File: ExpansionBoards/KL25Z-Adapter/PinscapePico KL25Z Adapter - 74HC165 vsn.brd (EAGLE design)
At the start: 82.6 x 53.1 mm, 26 parts, among them IC1 SN74HC165DR, IC2 SN74HC165DR, IC3 SN74HC165DR, IC4 LIS3DHTR, IC5 ADS1115IDGSR, IC6 PCA9555APW,118, SW1 TS-1187A-B-A-B

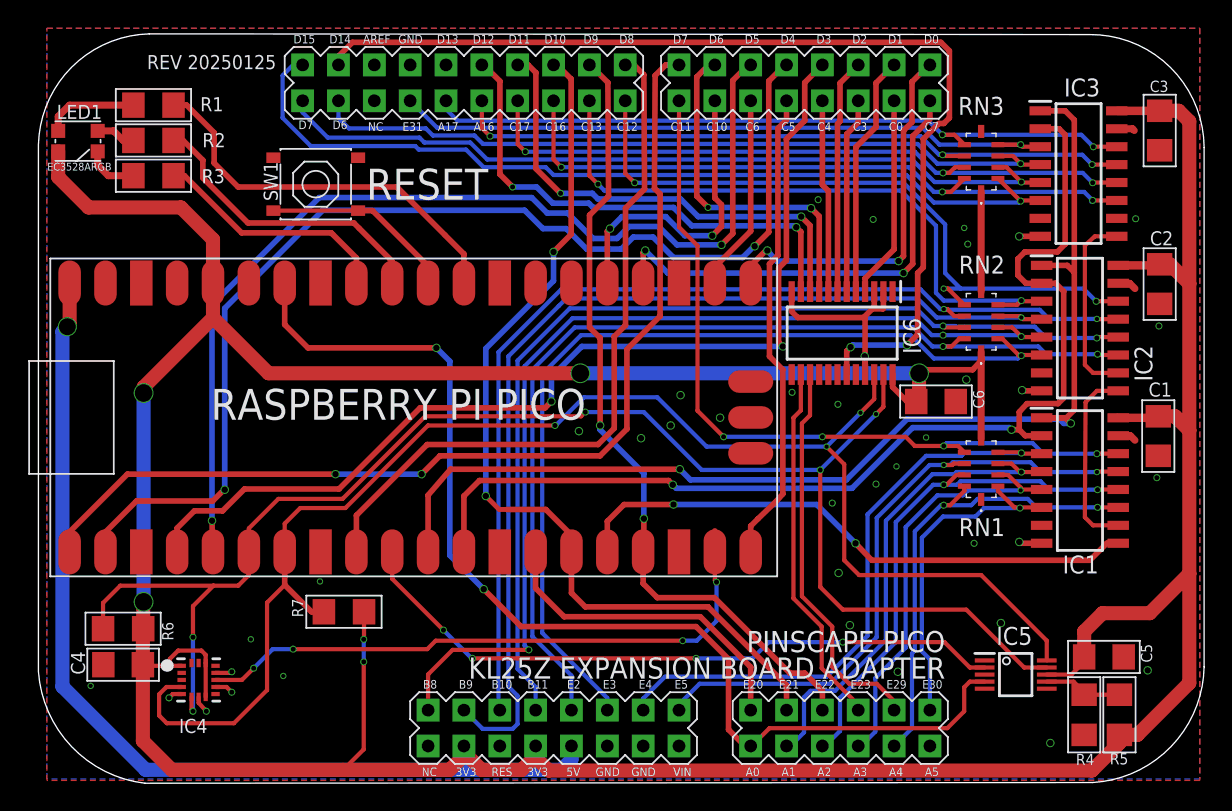
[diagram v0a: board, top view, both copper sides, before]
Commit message: Finish JSON configuration for 74HC165, tweaks to 74HC165 layout
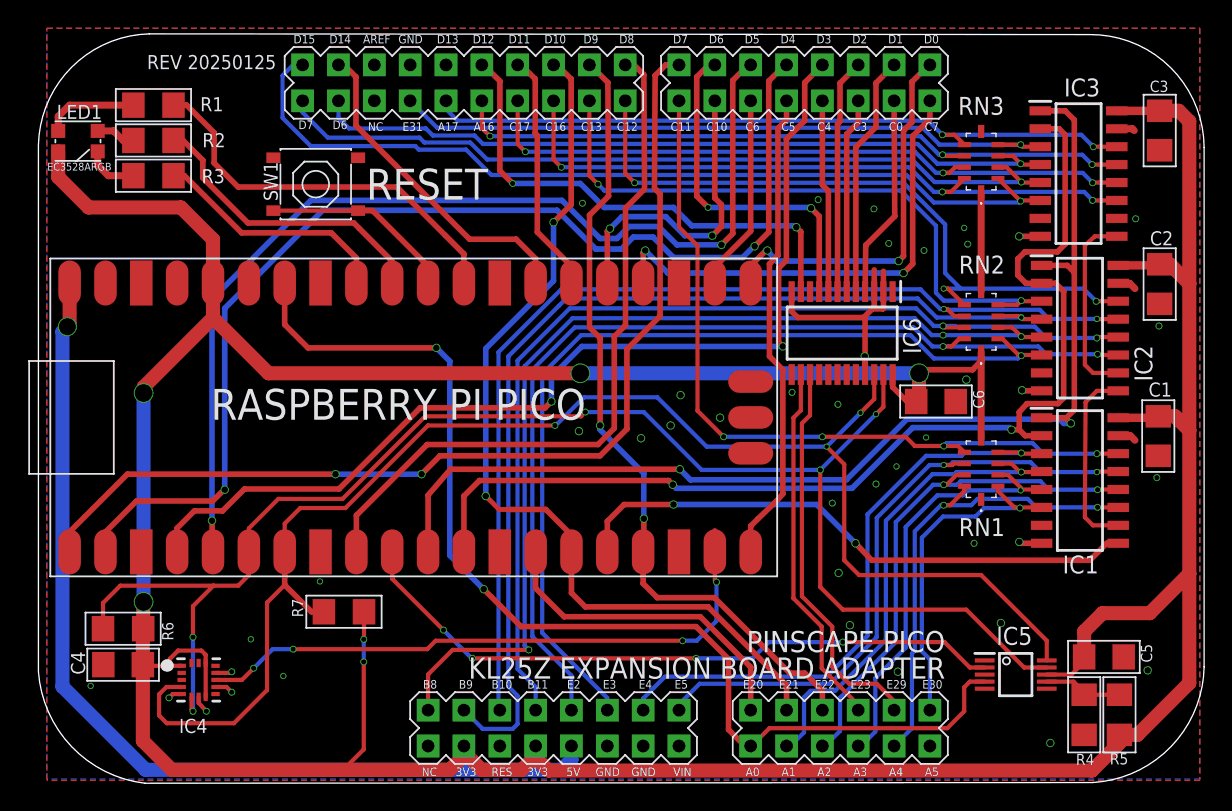
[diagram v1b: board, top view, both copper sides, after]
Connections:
- net PSU2_STATUS_SENSE: now also RASPBERRY_PI_PICO.GP20; no longer IC6.10
- net PSU2_STATUS_SET: now also RASPBERRY_PI_PICO.GP21; no longer IC6.19
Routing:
- net PSU2_STATUS_SET: track 73.0 -> 23.4 mm, vias 2 -> 0
- net PSU2_STATUS_SENSE: track 34.1 -> 17.2 mm, vias 2 -> 0
- net GND: track 29.0 -> 32.0 mm, vias 38 -> 41

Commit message: minor board updates
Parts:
- moved C5 2.81 mm to (75.7, 11.9)
- moved IC5 2.81 mm to (69.5, 10.7)
- moved R4 2.81 mm to (74.3, 7.80)
- moved R5 2.81 mm to (76.8, 7.80)
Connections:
- net BUTTON12: now also IC2.4, RN2.4; no longer IC2.13, RN2.8
- net BUTTON13: now also IC2.13, RN2.8; no longer IC2.4, RN2.4
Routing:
- net BUTTON12: track 73.7 -> 67.2 mm, vias 2 -> 1
- net PLUNGER_ADC: track 78.8 -> 81.8 mm
- net BUTTON13: track 72.6 -> 74.7 mm, vias 1 -> 2
- net 3V3_PICO: track 294.3 -> 296.3 mm, vias 6 -> 4
- net LED_B: track 28.3 -> 26.7 mm
- net PWM_GSCLK: track 27.4 -> 25.9 mm
- net SCL: track 104.8 -> 103.8 mm
- net CHIME_SCLK: track 80.7 -> 79.7 mm
- net PWM_XLAT: track 22.1 -> 22.7 mm
- net SDA: track 107.8 -> 107.2 mm
- net GND: vias 41 -> 45
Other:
- board text added: "REV 20250129"
- board text removed: "REV 20250125"

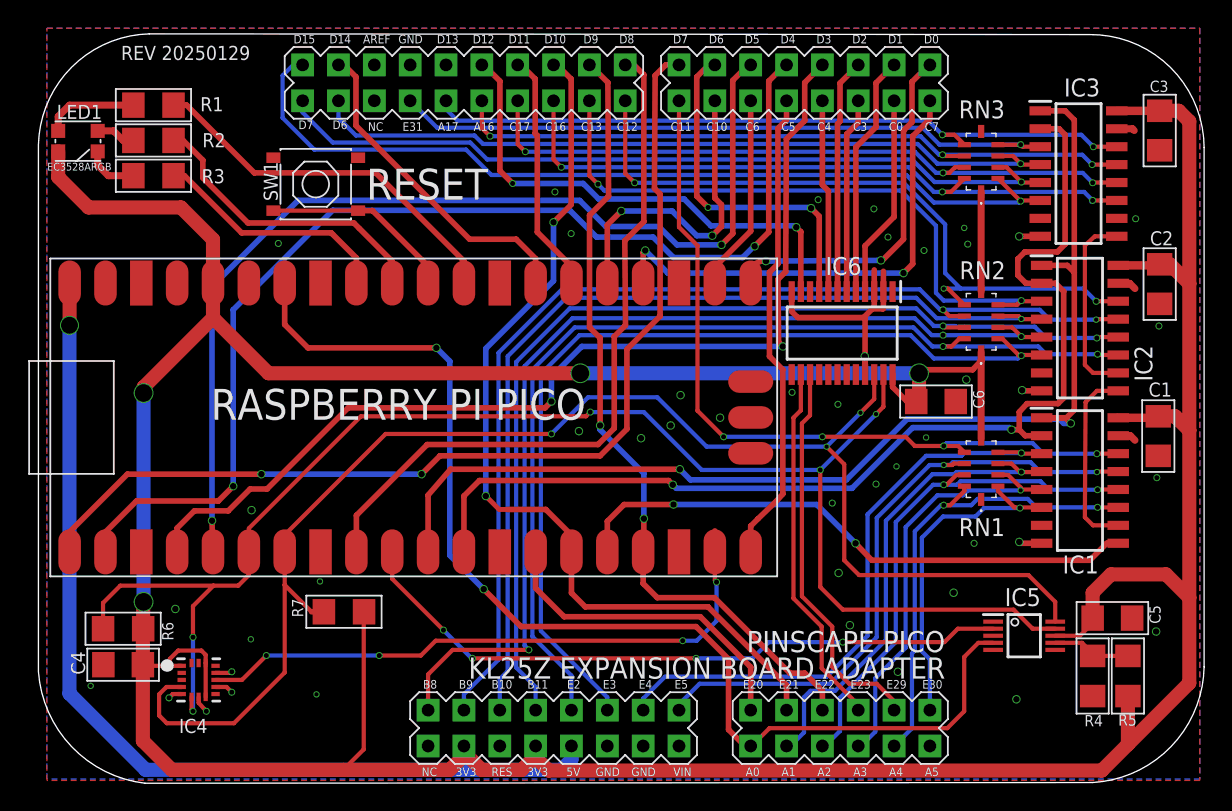
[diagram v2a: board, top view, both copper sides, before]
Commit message: THT version of the board design
- Changed Pico footprint to THT
- Relocated components
- Relayouted traces.
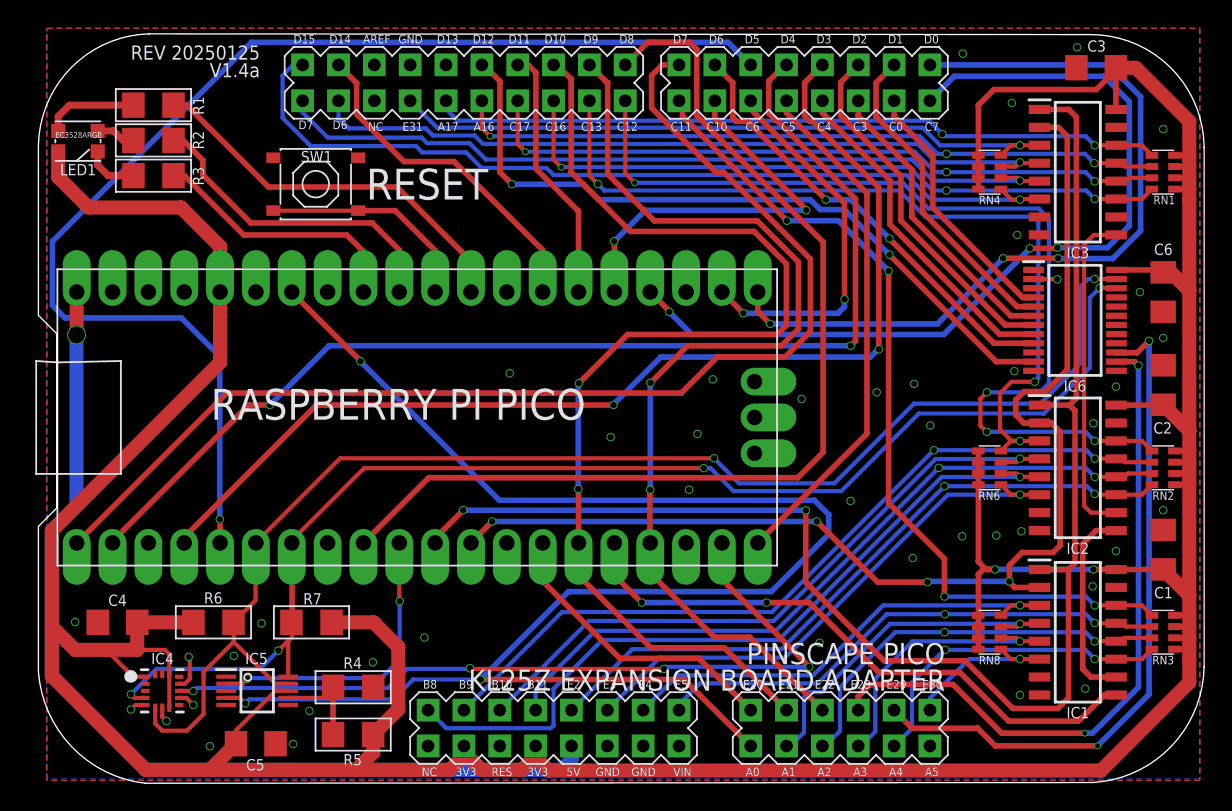
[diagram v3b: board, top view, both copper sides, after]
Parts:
- added RN4, RN6, RN8: CTS742C083, resistor-net:CTS742C083
- RASPBERRY_PI_PICO: device RaspberryPi_Pico:RPI_PICO -> RaspberryPi_Pico:RPI_PICO_TH
- RN1, RN2, RN3: value EXB-E10C103J -> CTS742C083; device SamacSys_Parts:EXBE10C103J -> resistor-net:CTS742C083
- moved C5 61.3 mm to (15.0, 3.00)
- moved R5 55.1 mm to (21.9, 3.65), turned to 180 degrees
- moved IC5 54.5 mm to (15.1, 6.75)
- moved R4 52.4 mm to (21.9, 7.00), turned to 180 degrees
- moved RN3 35.8 mm to (79.3, 10.9), turned to 270 degrees
- moved RN1 24.7 mm to (79.3, 43.5), turned to 270 degrees
- moved C6 17.9 mm to (79.3, 35.0), turned to 270 degrees
- moved RN2 16.5 mm to (79.3, 22.6), turned to 270 degrees
- moved IC6 16.5 mm to (73.0, 33.0), turned to 0 degrees
- moved IC1 10.8 mm to (73.2, 10.9)
- moved IC2 9.90 mm to (73.2, 22.6)
- moved C1 8.06 mm to (79.3, 16.8), turned to 90 degrees
- moved C2 7.15 mm to (79.3, 28.4), turned to 90 degrees
- moved R6 6.42 mm to (12.0, 11.6), turned to 0 degrees
- moved C3 6.33 mm to (74.5, 50.9), turned to 180 degrees
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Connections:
- removed net N$2: RN2.6, RN3.1
- net 3V3_PICO: now also RN1.5, RN1.7, RN1.8, RN2.5, RN2.6, RN2.7, RN2.8, RN3.5, RN3.6, RN3.7, RN3.8, RN4.1, RN4.2, RN4.3, RN4.4, RN6.1, RN6.2, RN6.3, RN6.4, RN8.1, RN8.2, RN8.3, RN8.4; no longer RN2.1
- net BUTTON1: now also RN3.4; no longer RN1.10
- net BUTTON10: now also RN2.4; no longer RN2.10
- net BUTTON11: now also RN2.3; no longer RN2.9
- net BUTTON12: now also RN6.7; no longer RN2.4
- net BUTTON13: now also RN2.2; no longer RN2.8
- net BUTTON14: now also RN6.6; no longer RN2.3
- net BUTTON15: now also RN2.1; no longer RN2.7
- net BUTTON16: now also RN6.8; no longer RN2.5
- net BUTTON17: now also RN1.4; no longer RN3.10
- net BUTTON18: now also RN1.3; no longer RN3.9
- net BUTTON19: now also RN1.2; no longer RN3.8
- net BUTTON2: now also RN8.6; no longer RN1.3
- net BUTTON20: now also RN1.1; no longer RN3.7
- net BUTTON21: now also RN4.8; no longer RN3.5
- net BUTTON22: now also RN4.7; no longer RN3.4
- net BUTTON23: now also RN4.6; no longer RN3.3
- net BUTTON24: now also RN4.5; no longer RN3.2
- net BUTTON3: now also RN3.3; no longer RN1.9
- net BUTTON4: now also RN8.7; no longer RN1.4
- net BUTTON5: now also RN8.5; no longer RN1.2
- net BUTTON6: now also RN3.1; no longer RN1.7
- net BUTTON7: now also RN3.2; no longer RN1.8
- net BUTTON8: now also RN8.8; no longer RN1.5
- net BUTTON9: now also RN6.5; no longer RN2.2
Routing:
- net PLUNGER_ADC: track 81.8 -> 114.9 mm, vias 2 -> 3
- net PWM_GSCLK: track 25.9 -> 57.0 mm, vias 2 -> 3
- net PWM_BLANK: track 34.3 -> 62.8 mm, vias 2 -> 3
- net BUTTON9: track 65.4 -> 38.6 mm
- net ADC_INTR: track 47.7 -> 21.3 mm, vias 4 -> 2
- net GND: track 32.0 -> 7.61 mm, vias 45 -> 43
- net PLUNGER_CAL_LED: track 25.9 -> 48.4 mm, vias 0 -> 2
- net IR_IN: track 51.0 -> 73.4 mm
- net BUTTON10: track 70.7 -> 48.9 mm
- net BUTTON_SHLD: track 83.1 -> 103.9 mm
- net PLUNGER_CAL_BTN: track 27.9 -> 48.4 mm, vias 0 -> 2
- net BUTTON12: track 67.2 -> 47.1 mm
- net BUTTON11: track 72.0 -> 52.0 mm
- net BUTTON15: track 49.6 -> 68.9 mm, vias 3 -> 4
- net BUTTON13: track 74.7 -> 56.7 mm
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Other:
- outline, holes or cut-outs redrawn
- board text added: "REV 20250125 V1.4a"
- board text removed: "REV 20250129"

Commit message: KL25Z adapter layout tweaks
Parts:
- RASPBERRY_PI_PICO: device RaspberryPi_Pico:RPI_PICO_TH -> RaspberryPi_Pico:RPI_PICO_TH_NO_DEBUG
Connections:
- net GND: no longer RASPBERRY_PI_PICO.GND@5
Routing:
- net PWM_GSCLK: track 57.0 -> 33.7 mm, vias 3 -> 1
- net PWM_BLANK: track 62.8 -> 44.1 mm, vias 3 -> 1
- net ACCEL_INTR: track 56.8 -> 44.8 mm, vias 4 -> 1
- net BUTTON15: track 68.9 -> 61.6 mm, vias 4 -> 2
- net GND: track 7.61 -> 10.8 mm, vias 43 -> 64
- net PWM_SIN: track 26.9 -> 24.2 mm, vias 2 -> 1
- net PLUNGER_SDA: track 21.2 -> 23.2 mm
- net PLUNGER_IRQ1_SCL: track 79.3 -> 80.7 mm
- net PLUNGER_ADC: track 114.9 -> 114.2 mm, vias 3 -> 6
- net PLUNGER_CAL_LED: track 48.4 -> 49.1 mm
- net BUTTON_DATA: track 42.9 -> 43.6 mm
- net BUTTON_SHLD: track 103.9 -> 103.3 mm, vias 2 -> 1
- net PLUNGER_IRQ2: track 70.9 -> 71.5 mm
- net BUTTON_CLK: track 84.3 -> 84.1 mm, vias 4 -> 3
- net PWM_XLAT: track 28.5 -> 28.7 mm, vias 2 -> 1
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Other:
- board text added: "REV 20250201"
- board text removed: "REV 20250125 V1.4a"

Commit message: KL25Z adapters - connect AGND to GND
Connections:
- net GND: now also RASPBERRY_PI_PICO.AGND
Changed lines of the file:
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@@
 <via x="64.35" y="5.1" extent="1-16" drill="0.35"/>
 <via x="33.75" y="8.075" extent="1-16" drill="0.45"/>
+<contactref element="RASPBERRY_PI_PICO" pad="AGND"/>
 </signal>
 <signal name="SDA">

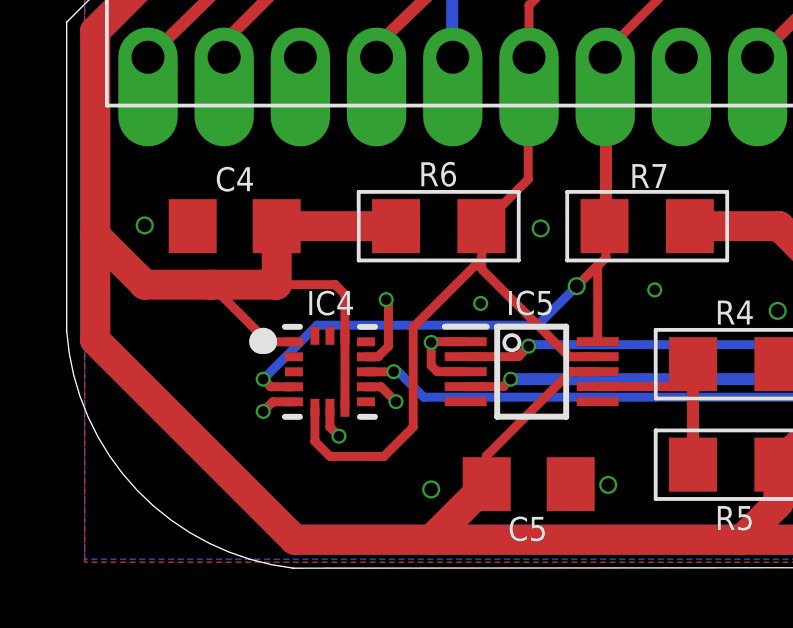
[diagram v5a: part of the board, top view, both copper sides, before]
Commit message: Update Pro and KL25Z adapter boards to make LIS3DH footprint compatible with LIS3DSH
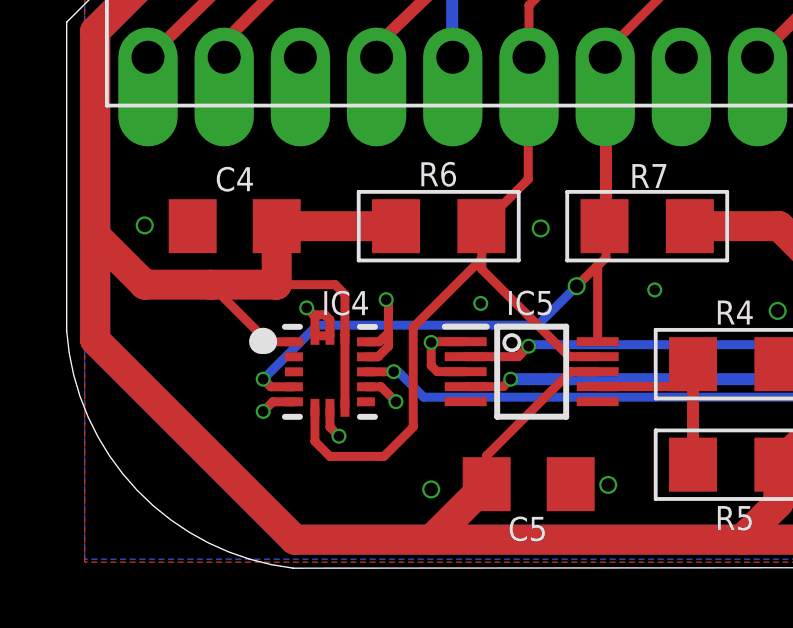
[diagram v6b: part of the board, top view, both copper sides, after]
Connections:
- net GND: now also IC4.13, IC4.15, IC4.16
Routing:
- net GND: track 10.8 -> 14.3 mm, vias 64 -> 65
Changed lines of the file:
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@@
 <attribute name="MOUSER_PART_NUMBER" value="511-LIS3DHTR" x="7.105" y="6.745" size="1.778" layer="27" display="off"/>
 <attribute name="MOUSER_PRICE-STOCK" value="https://www.mouser.co.uk/ProductDetail/STMicroelectronics/LIS3DHTR?qs=6la6oa3D8xzhXYax3cEo4w%3D%3D" x="7.105" y="6.745" size="1.778" layer="27" display="off"/>
-<attribute name="NAME" x="8.394" y="9.035" size="0.8" layer="25" align="center"/>
+<attribute name="NAME" x="8.894" y="9.035" size="0.8" layer="25" align="center"/>
 <attribute name="VALUE" x="8.394" y="4.405" size="0.7" layer="27" align="center"/>
 </element>
@@
 <wire x1="9.575" y1="7.245" x2="9.975" y2="7.245" width="0.3" layer="1"/>
 <wire x1="10.25" y1="9.15" x2="10.325" y2="9.075" width="0.3" layer="1"/>
-<wire x1="10.325" y1="9.075" x2="10.325" y2="7.595" width="0.3" layer="1"/>
+<wire x1="10.325" y1="9.075" x2="10.325" y2="8.05" width="0.3" layer="1"/>
 <via x="8.675" y="4.6" extent="1-16" drill="0.35"/>
 <via x="10.25" y="9.15" extent="1-16" drill="0.35"/>
 <via x="10.575" y="5.75" extent="1-16" drill="0.35"/>
 <contactref element="IC4" pad="7"/>
+<wire x1="10.325" y1="8.05" x2="10.325" y2="7.595" width="0.3" layer="1"/>
 <wire x1="8.375" y1="5.545" x2="8.375" y2="4.9" width="0.3" layer="1"/>
 <wire x1="8.675" y1="4.6" x2="8.375" y2="4.9" width="0.3" layer="1"/>
@@
 <via x="33.75" y="8.075" extent="1-16" drill="0.45"/>
 <contactref element="RASPBERRY_PI_PICO" pad="AGND"/>
+<contactref element="IC4" pad="13"/>
+<contactref element="IC4" pad="15"/>
+<contactref element="IC4" pad="16"/>
+<wire x1="9.575" y1="7.745" x2="10.02" y2="7.745" width="0.3" layer="1"/>
+<wire x1="10.02" y1="7.745" x2="10.325" y2="8.05" width="0.3" layer="1"/>
+<via x="7.6" y="8.875" extent="1-16" drill="0.35"/>
+<wire x1="7.875" y1="7.945" x2="7.875" y2="8.6" width="0.3" layer="1"/>
+<wire x1="7.875" y1="8.6" x2="7.827603125" y2="8.647396875" width="0.3" layer="1"/>
+<wire x1="7.827603125" y1="8.647396875" x2="7.6" y2="8.875" width="0.3" layer="1"/>
+<wire x1="7.875" y1="7.945" x2="8.375" y2="7.945" width="0.3" layer="1"/>
+<wire x1="8.375" y1="7.945" x2="8.375" y2="8.475" width="0.3" layer="1"/>
+<wire x1="8.375" y1="8.475" x2="8.202603125" y2="8.647396875" width="0.3" layer="1"/>
+<wire x1="7.827603125" y1="8.647396875" x2="8.202603125" y2="8.647396875" width="0.3" layer="1"/>
 </signal>
 <signal name="SDA">
